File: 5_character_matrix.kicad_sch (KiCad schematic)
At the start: 17 parts, among them U1 SM411006N/15, U2 SN74LVC244A, U3 SM411006N/15, U4 SM411006N/15, U5 SN74LVC244A, U6 SM411006N/15, U7 SM411006N/15

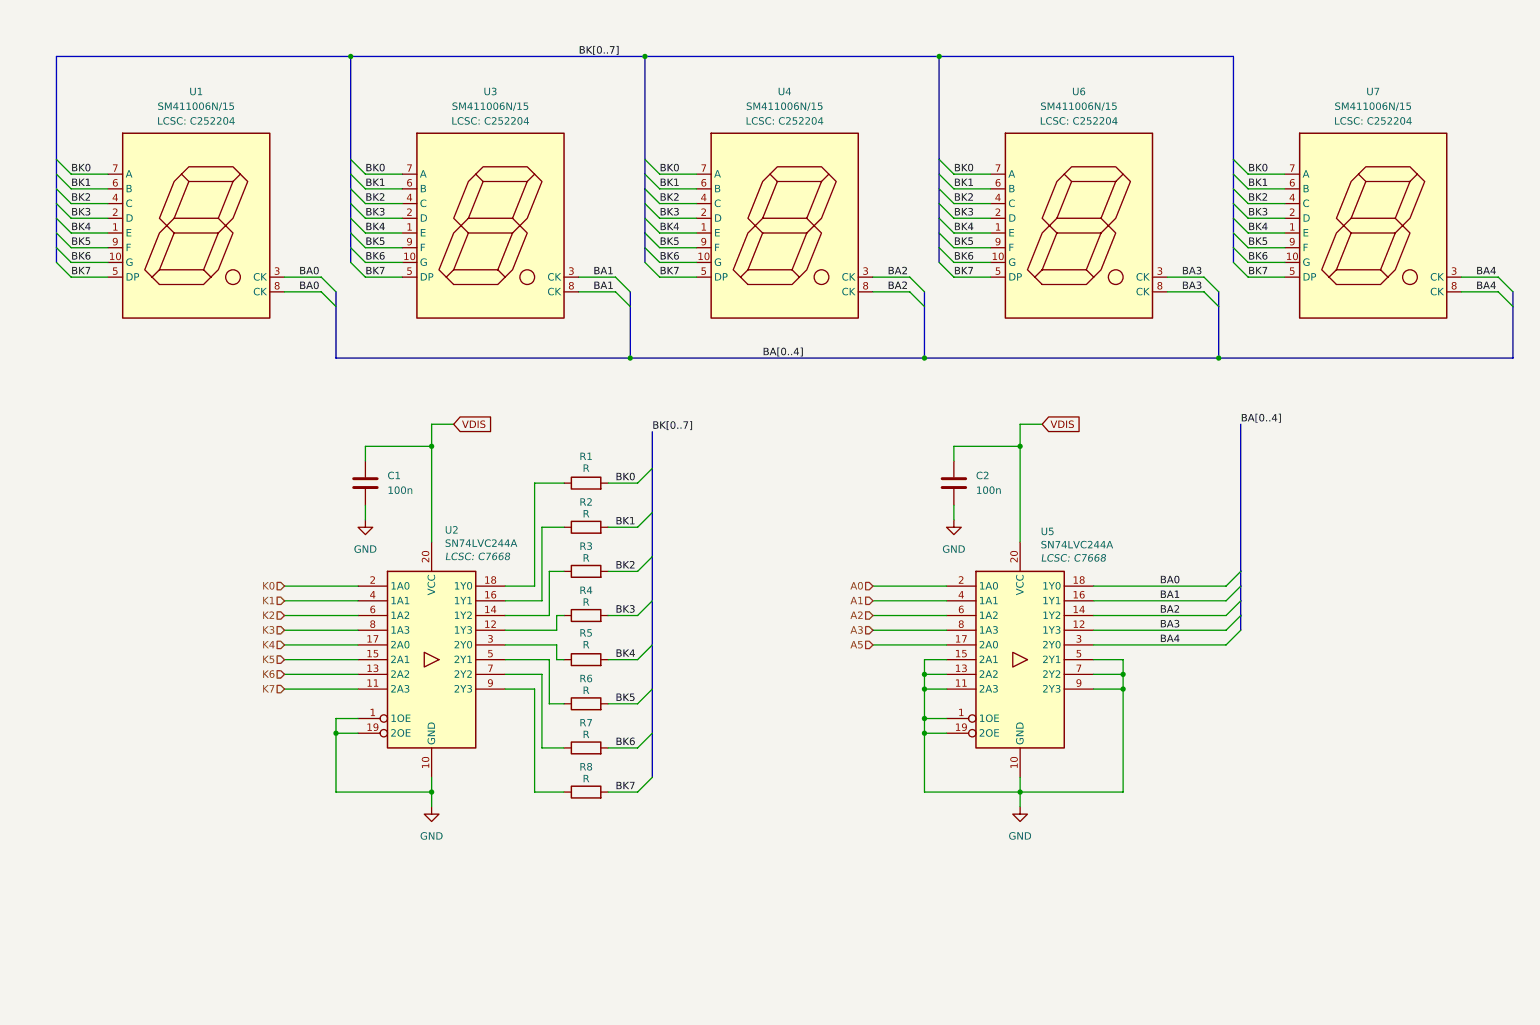
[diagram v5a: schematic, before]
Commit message: current limit resistors
- styling changes in the schematics
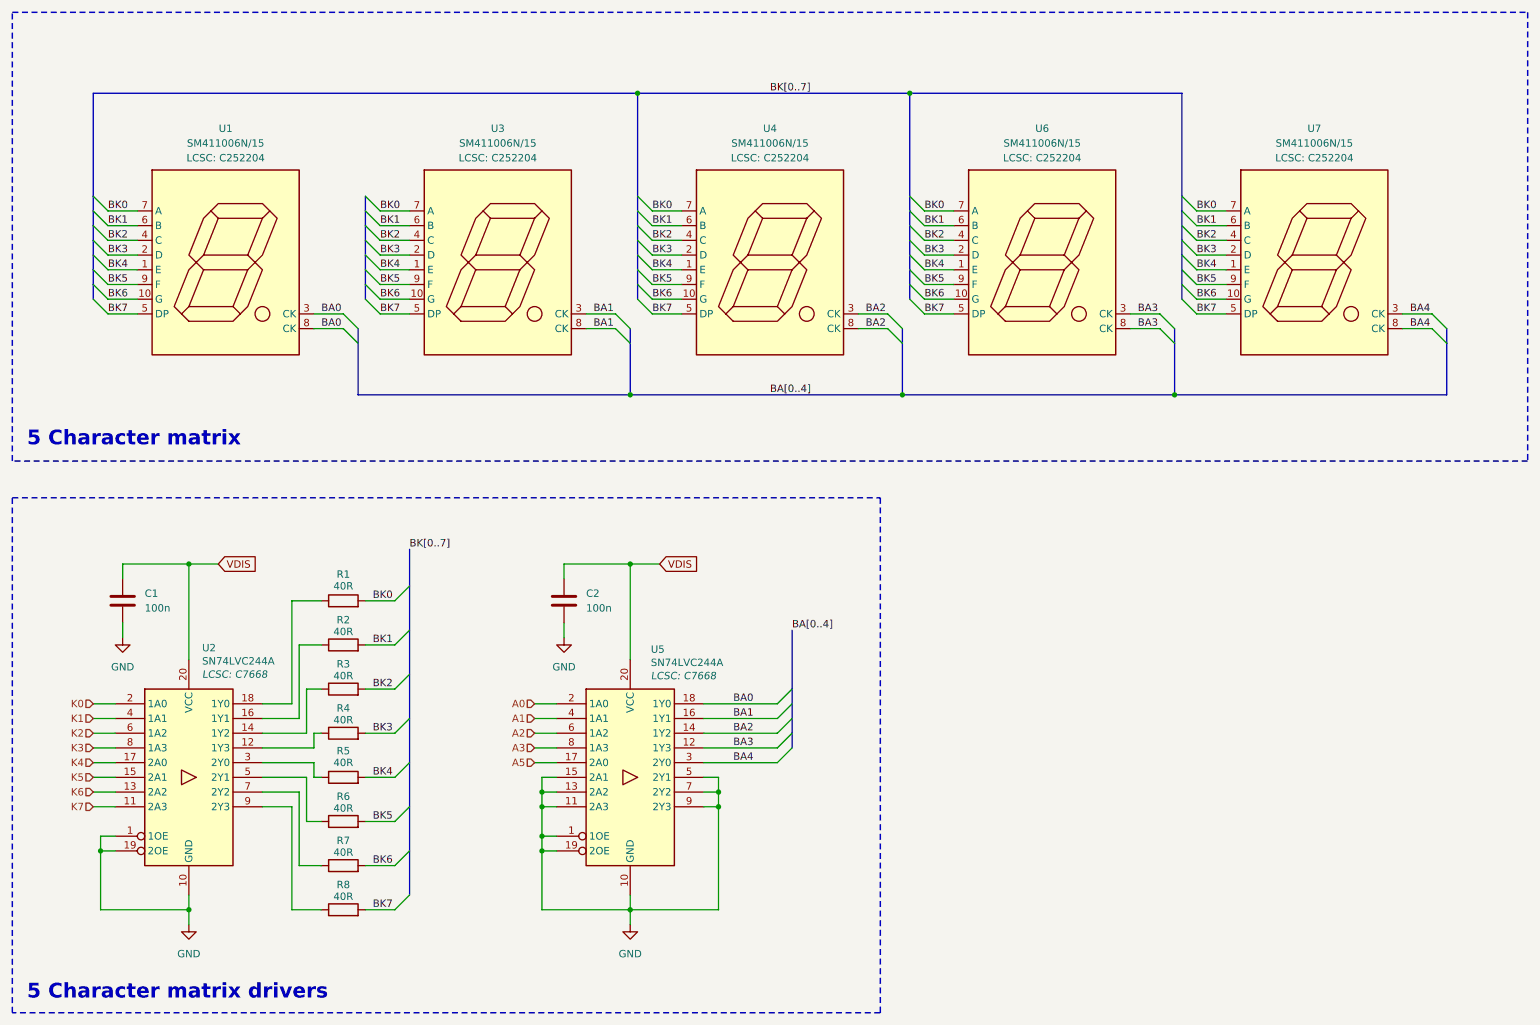
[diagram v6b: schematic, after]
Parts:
- R1, R2, R3, R4, R5, R6, R7, R8: value R -> 40R
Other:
- note added: "5 Character matrix"
- note added: "5 Character matrix drivers"
- moved on the sheet: C1, C2, R1, R2, R3, R4, R5, R6, R7, R8, U1, U2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

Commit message: minor changes
- removal of colon LEDs
- removal of test points addition of solders bridges
- time pulse LED added
- modification in MCU pinout
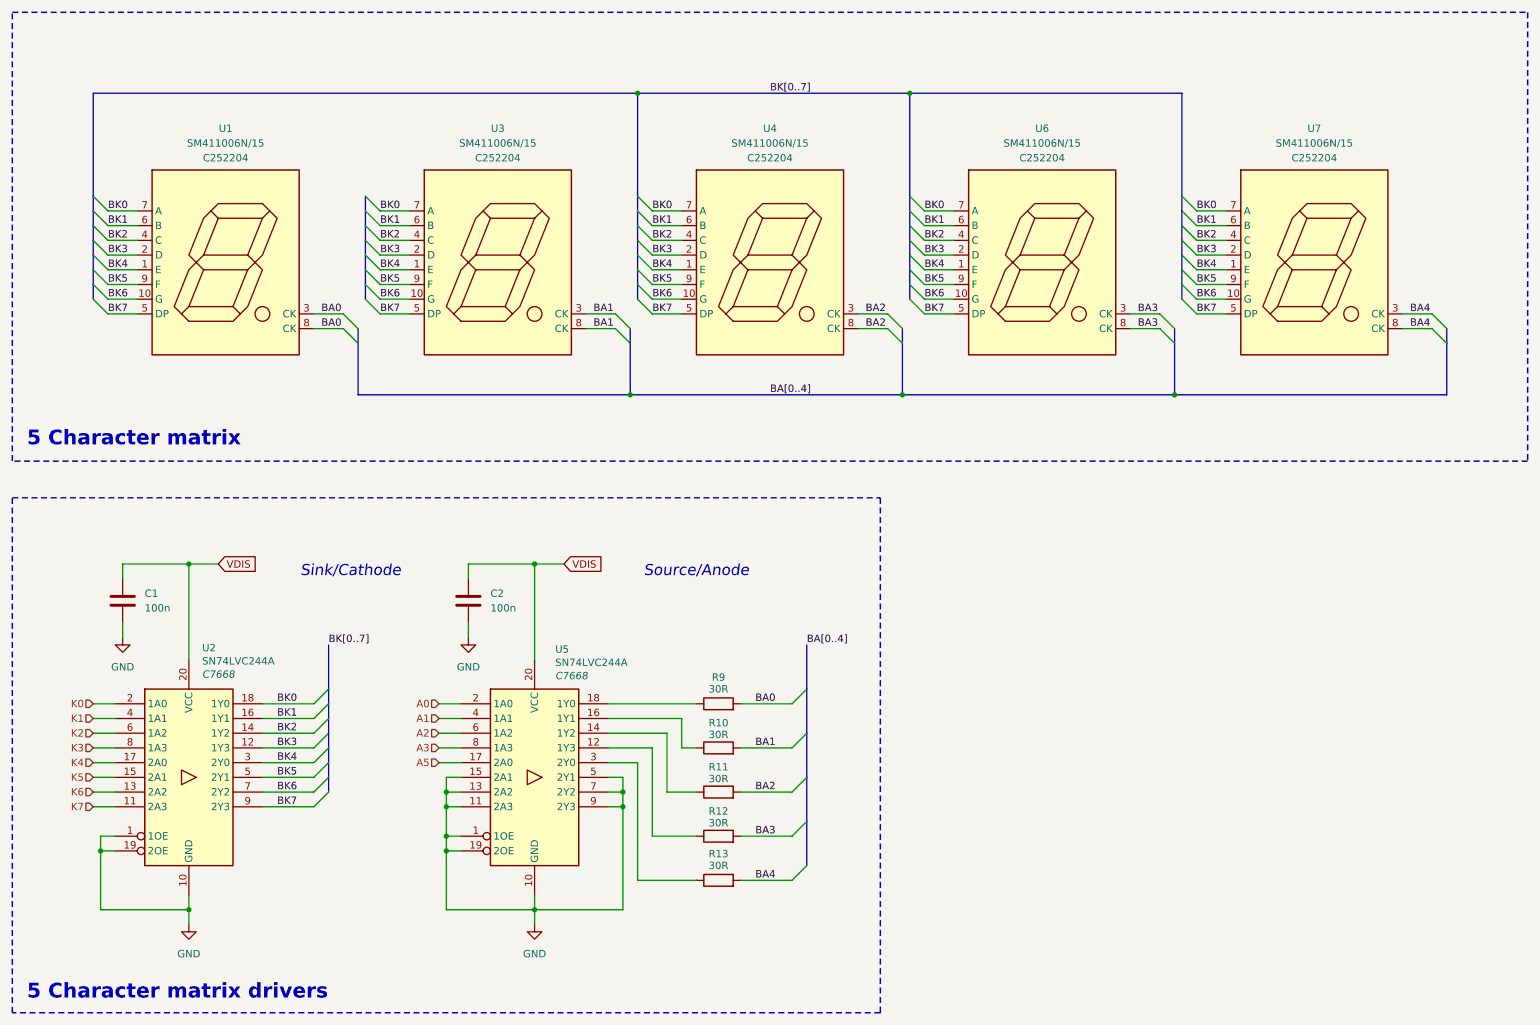
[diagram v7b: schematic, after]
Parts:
- removed R6, R7, R8: 40R, symbol Device:R
- R10: renamed from R2; value 40R -> 30R
- R11: renamed from R3; value 40R -> 30R
- R12: renamed from R4; value 40R -> 30R
- R13: renamed from R5; value 40R -> 30R
- R9: renamed from R1; value 40R -> 30R
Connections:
- net BA0: now also R9.2; no longer U5.18 (1Y0)
- net BA1: now also R10.2; no longer U5.16 (1Y1)
- net BA2: now also R11.2; no longer U5.14 (1Y2)
- net BA3: now also R12.2; no longer U5.12 (1Y3)
- net BA4: now also R13.2; no longer U5.3 (2Y0)
- net BK0: now also U2.18 (1Y0); no longer R9.2
- net BK1: now also U2.16 (1Y1); no longer R10.2
- net BK2: now also U2.14 (1Y2); no longer R11.2
- net BK3: now also U2.12 (1Y3); no longer R12.2
- net BK4: now also U2.3 (2Y0); no longer R13.2
- net BK5: now also U2.5 (2Y1)
- net BK6: now also U2.7 (2Y2)
- net BK7: now also U2.9 (2Y3)
- net at R12.1: now also U5.12 (1Y3); no longer U2.12 (1Y3)
- net at R10.1: now also U5.16 (1Y1); no longer U2.16 (1Y1)
- net at R11.1: now also U5.14 (1Y2); no longer U2.14 (1Y2)
- net at R9.1: now also U5.18 (1Y0); no longer U2.18 (1Y0)
- net at R13.1: now also U5.3 (2Y0); no longer U2.3 (2Y0)
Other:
- note added: "Sink/Cathode"
- note added: "Source/Anode"
- title: (none) -> 5 Character Matrix & Drivers 
- moved on the sheet: C2, R10, R11, R12, R13, R9, U5

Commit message: minor changes
- annotations added
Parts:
- renumbered R9 to R1, R10 to R2, R11 to R3, R12 to R4, R13 to R5, U2 to U1, U1 to U2, U5 to U4, U4 to U5
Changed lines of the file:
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@@
 	(title_block
 		(title "5 Character Matrix & Drivers ")
-		(date "2025-10-22")
+		(date "2025-10-19")
 		(rev "v0.0")
 		(company "Rajath Katker")
@@
 			(font
 				(size 2.54 2.54)
-				(thickness 0.508)
-				(bold yes)
+				(thickness 0.3175)
 				(color 194 0 0 1)
 			)
@@
 			(font
 				(size 2.54 2.54)
-				(thickness 0.508)
-				(bold yes)
+				(thickness 0.3175)
 				(color 194 0 0 1)
 			)
@@
 		(on_board yes)
 		(dnp no)
-		(property "Reference" "R12"
+		(property "Reference" "R4"
 			(at 139.7 155.702 90)
 			(effects
@@
 			(project "Precision Clock"
 				(path "/c9a8ff63-a0d1-4125-9dd1-40fb53daf536/61b252ee-6ab4-4417-a4ad-7fc052d7ca20"
-					(reference "R12")
+					(reference "R14")
 					(unit 1)
 				)
 				(path "/c9a8ff63-a0d1-4125-9dd1-40fb53daf536/95a63663-b2f9-448f-a4dd-b71321e8f379"
-					(reference "R12")
+					(reference "R4")
 					(unit 1)
 				)
 				(path "/c9a8ff63-a0d1-4125-9dd1-40fb53daf536/e0daf664-e239-498f-ad2e-96c4213a6fbd"
-					(reference "R12")
+					(reference "R9")
 					(unit 1)
 				)
@@
 		(on_board yes)
 		(dnp no)
-		(property "Reference" "R10"
+		(property "Reference" "R2"
 			(at 139.7 140.462 90)
 			(effects
@@
 			(project "Precision Clock"
 				(path "/c9a8ff63-a0d1-4125-9dd1-40fb53daf536/61b252ee-6ab4-4417-a4ad-7fc052d7ca20"
-					(reference "R10")
+					(reference "R12")
 					(unit 1)
 				)
 				(path "/c9a8ff63-a0d1-4125-9dd1-40fb53daf536/95a63663-b2f9-448f-a4dd-b71321e8f379"
-					(reference "R10")
+					(reference "R2")
 					(unit 1)
 				)
 				(path "/c9a8ff63-a0d1-4125-9dd1-40fb53daf536/e0daf664-e239-498f-ad2e-96c4213a6fbd"
-					(reference "R10")
+					(reference "R7")
 					(unit 1)
 				)
@@
 		(on_board yes)
 		(dnp no)
-		(property "Reference" "U4"
+		(property "Reference" "U5"
 			(at 148.59 37.846 0)
 			(effects
@@
 			(project "Precision Clock"
 				(path "/c9a8ff63-a0d1-4125-9dd1-40fb53daf536/61b252ee-6ab4-4417-a4ad-7fc052d7ca20"
-					(reference "U18")
+					(reference "U19")
 					(unit 1)
 				)
 				(path "/c9a8ff63-a0d1-4125-9dd1-40fb53daf536/95a63663-b2f9-448f-a4dd-b71321e8f379"
-					(reference "U4")
+					(reference "U5")
 					(unit 1)
 				)
 				(path "/c9a8ff63-a0d1-4125-9dd1-40fb53daf536/e0daf664-e239-498f-ad2e-96c4213a6fbd"
-					(reference "U11")
+					(reference "U12")
 					(unit 1)
 				)
@@
 		(on_board yes)
 		(dnp no)
-		(property "Reference" "U2"
+		(property "Reference" "U1"
 			(at 50.546 127.508 0)
 			(effects
@@
 			(project "Precision Clock"
 				(path "/c9a8ff63-a0d1-4125-9dd1-40fb53daf536/61b252ee-6ab4-4417-a4ad-7fc052d7ca20"
-					(reference "U16")
+					(reference "U15")
 					(unit 1)
 				)
 				(path "/c9a8ff63-a0d1-4125-9dd1-40fb53daf536/95a63663-b2f9-448f-a4dd-b71321e8f379"
-					(reference "U2")
+					(reference "U1")
 					(unit 1)
 				)
 				(path "/c9a8ff63-a0d1-4125-9dd1-40fb53daf536/e0daf664-e239-498f-ad2e-96c4213a6fbd"
-					(reference "U9")
+					(reference "U8")
 					(unit 1)
 				)
@@
 		(on_board yes)
 		(dnp no)
-		(property "Reference" "U5"
+		(property "Reference" "U4"
 			(at 111.506 127.762 0)
 			(effects
@@
 			(project "Precision Clock"
 				(path "/c9a8ff63-a0d1-4125-9dd1-40fb53daf536/61b252ee-6ab4-4417-a4ad-7fc052d7ca20"
-					(reference "U19")
+					(reference "U18")
 					(unit 1)
 				)
 				(path "/c9a8ff63-a0d1-4125-9dd1-40fb53daf536/95a63663-b2f9-448f-a4dd-b71321e8f379"
-					(reference "U5")
+					(reference "U4")
 					(unit 1)
 				)
 				(path "/c9a8ff63-a0d1-4125-9dd1-40fb53daf536/e0daf664-e239-498f-ad2e-96c4213a6fbd"
-					(reference "U12")
+					(reference "U11")
 					(unit 1)
 				)
@@
 		(on_board yes)
 		(dnp no)
-		(property "Reference" "U1"
+		(property "Reference" "U2"
 			(at 54.61 37.846 0)
 			(effects
@@
 			(project ""
 				(path "/c9a8ff63-a0d1-4125-9dd1-40fb53daf536/61b252ee-6ab4-4417-a4ad-7fc052d7ca20"
-					(reference "U15")
+					(reference "U16")
 					(unit 1)
 				)
 				(path "/c9a8ff63-a0d1-4125-9dd1-40fb53daf536/95a63663-b2f9-448f-a4dd-b71321e8f379"
-					(reference "U1")
+					(reference "U2")
 					(unit 1)
 				)
 				(path "/c9a8ff63-a0d1-4125-9dd1-40fb53daf536/e0daf664-e239-498f-ad2e-96c4213a6fbd"
-					(reference "U8")
+					(reference "U9")
 					(unit 1)
 				)
@@
 		(on_board yes)
 		(dnp no)
-		(property "Reference" "R13"
+		(property "Reference" "R5"
 			(at 139.7 163.068 90)
 			(effects
@@
 			(project "Precision Clock"
 				(path "/c9a8ff63-a0d1-4125-9dd1-40fb53daf536/61b252ee-6ab4-4417-a4ad-7fc052d7ca20"
-					(reference "R13")
+					(reference "R15")
 					(unit 1)
 				)
 				(path "/c9a8ff63-a0d1-4125-9dd1-40fb53daf536/95a63663-b2f9-448f-a4dd-b71321e8f379"
-					(reference "R13")
+					(reference "R5")
 					(unit 1)
 				)
 				(path "/c9a8ff63-a0d1-4125-9dd1-40fb53daf536/e0daf664-e239-498f-ad2e-96c4213a6fbd"
-					(reference "R13")
+					(reference "R10")
 					(unit 1)
 				)
@@
 		(on_board yes)
 		(dnp no)
-		(property "Reference" "R9"
+		(property "Reference" "R1"
 			(at 139.7 132.588 90)
 			(effects
@@
 			(project "Precision Clock"
 				(path "/c9a8ff63-a0d1-4125-9dd1-40fb53daf536/61b252ee-6ab4-4417-a4ad-7fc052d7ca20"
-					(reference "R9")
+					(reference "R11")
 					(unit 1)
 				)
 				(path "/c9a8ff63-a0d1-4125-9dd1-40fb53daf536/95a63663-b2f9-448f-a4dd-b71321e8f379"
-					(reference "R9")
+					(reference "R1")
 					(unit 1)
 				)
 				(path "/c9a8ff63-a0d1-4125-9dd1-40fb53daf536/e0daf664-e239-498f-ad2e-96c4213a6fbd"
-					(reference "R9")
+					(reference "R6")
 					(unit 1)
 				)
@@
 		(on_board yes)
 		(dnp no)
-		(property "Reference" "R11"
+		(property "Reference" "R3"
 			(at 139.7 148.082 90)
 			(effects
@@
 			(project "Precision Clock"
 				(path "/c9a8ff63-a0d1-4125-9dd1-40fb53daf536/61b252ee-6ab4-4417-a4ad-7fc052d7ca20"
-					(reference "R11")
+					(reference "R13")
 					(unit 1)
 				)
 				(path "/c9a8ff63-a0d1-4125-9dd1-40fb53daf536/95a63663-b2f9-448f-a4dd-b71321e8f379"
-					(reference "R11")
+					(reference "R3")
 					(unit 1)
 				)
 				(path "/c9a8ff63-a0d1-4125-9dd1-40fb53daf536/e0daf664-e239-498f-ad2e-96c4213a6fbd"
-					(reference "R11")
+					(reference "R8")
 					(unit 1)
 				)
